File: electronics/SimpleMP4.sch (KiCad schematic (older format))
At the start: 124 parts, among them J1 USB_OTG, J2 DISPLAY, Q1 8050, Q2 SI2305, Q3 SI2305, Q4 8050, Q5 8550, Q6 SI2305, Q7 8550, U1 OCP8020, U2 RK2608, U3 OCP2150TW18A, U4 OCP1240, U5 MT25QL128ABA, U6 K9HCG08U1M-PCB0/PIB0, U7 K4S641632N, U8 TRS_5PIN, U9 MMC/SD_SOCKET, Y1 24MHz

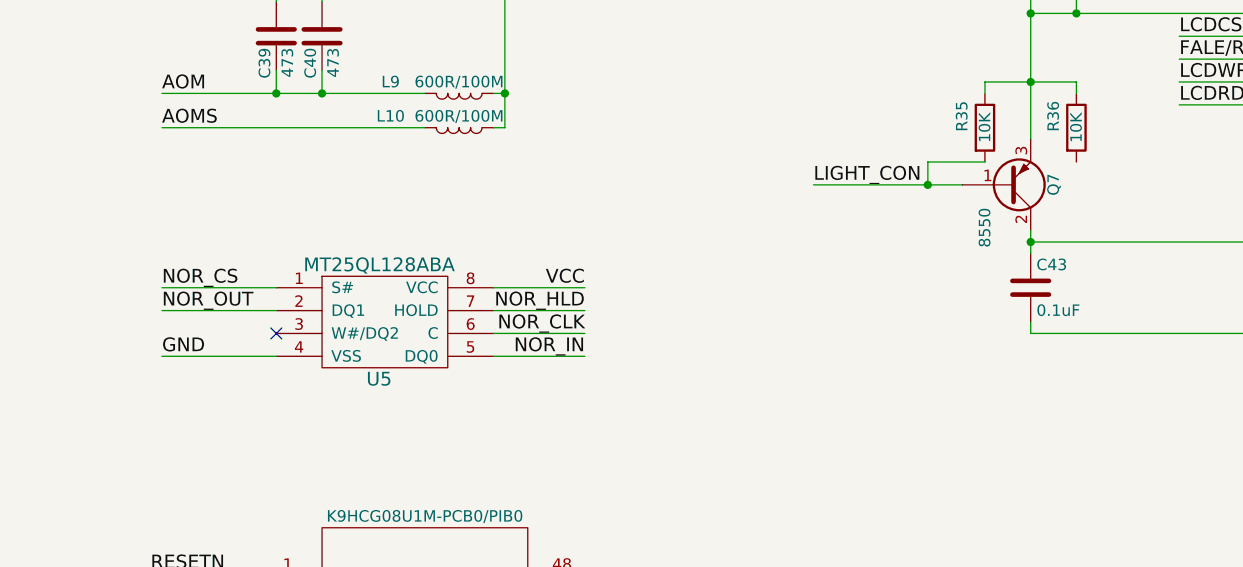
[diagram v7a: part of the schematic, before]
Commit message: fixed error in schematics
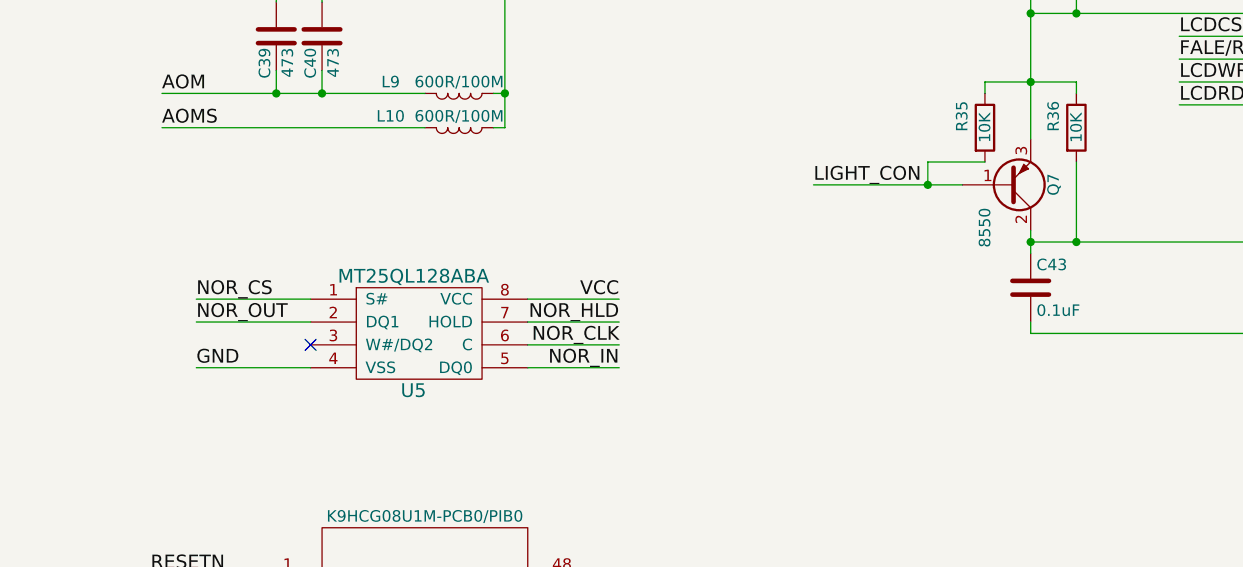
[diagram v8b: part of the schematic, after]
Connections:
- net at C43.1, J2.16 (P16), Q7.2 (C): now also R36.2
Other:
- moved on the sheet: U5
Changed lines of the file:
@@
 L MT25QL128ABA U5
 U 1 1 5A3C15DE
-P 10150 3400
-F 0 "U5" H 10200 3350 60  0000 C CNN
-F 1 "MT25QL128ABA" H 10200 3850 60  0000 C CNN
-F 2 "" H 10150 3000 60  0001 C CNN
-F 3 "" H 10150 3000 60  0001 C CNN
-	1    10150 3400
+P 10300 3450
+F 0 "U5" H 10350 3400 60  0000 C CNN
+F 1 "MT25QL128ABA" H 10350 3900 60  0000 C CNN
+F 2 "" H 10300 3050 60  0001 C CNN
+F 3 "" H 10300 3050 60  0001 C CNN
+	1    10300 3450
 	1    0    0    -1
 $EndComp
-Text Label 11100 3050 2    60   ~ 0
+Text Label 11250 3100 2    60   ~ 0
 VCC
-Text Label 9250 3350 0    60   ~ 0
+Text Label 9400 3400 0    60   ~ 0
 GND
-Text Label 11100 3350 2    60   ~ 0
+Text Label 11250 3400 2    60   ~ 0
 NOR_IN
-Text Label 9250 3150 0    60   ~ 0
+Text Label 9400 3200 0    60   ~ 0
 NOR_OUT
-Text Label 11100 3250 2    60   ~ 0
+Text Label 11250 3300 2    60   ~ 0
 NOR_CLK
-NoConn ~ 9750 3250
-Text Label 11100 3150 2    60   ~ 0
+NoConn ~ 9900 3300
+Text Label 11250 3200 2    60   ~ 0
 NOR_HLD
-Text Label 9250 3050 0    60   ~ 0
+Text Label 9400 3100 0    60   ~ 0
 NOR_CS
 Text Label 7200 5250 0    60   ~ 0
@@
 	9250 2350 10400 2350
 Wire Wire Line
-	10700 3050 11100 3050
-Wire Wire Line
-	9750 3350 9250 3350
-Wire Wire Line
-	10700 3350 11100 3350
-Wire Wire Line
-	9750 3150 9250 3150
-Wire Wire Line
-	10700 3250 11100 3250
-Wire Wire Line
-	10700 3150 11100 3150
-Wire Wire Line
-	9750 3050 9250 3050
+	10850 3100 11250 3100
+Wire Wire Line
+	9900 3400 9400 3400
+Wire Wire Line
+	10850 3400 11250 3400
+Wire Wire Line
+	9900 3200 9400 3200
+Wire Wire Line
+	10850 3300 11250 3300
+Wire Wire Line
+	10850 3200 11250 3200
+Wire Wire Line
+	9900 3100 9400 3100
 Wire Wire Line
 	13700 1950 14250 1950
@@
 	13800 4400 14350 4400
 Connection ~ 14050 4400
+Wire Wire Line
+	13250 2500 13250 2850
+Connection ~ 13250 2850
 $EndSCHEMATC
